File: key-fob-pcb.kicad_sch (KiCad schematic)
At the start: 1 part

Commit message: layout complete
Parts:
- removed BT1: 2468, 2468:BAT_2468, symbol 2468:2468
- added BT1: AAAx2, Connector_PinHeader_2.54mm:PinHeader_1x02_P2.54mm_Vertical, symbol Device:Battery
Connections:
- net ADC/VIN: now also BT1.1 (+)
- net GND: now also BT1.2 (-)
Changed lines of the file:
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@@
   (junction (at 62.23 46.99) (diameter 0) (color 0 0 0 0)
   )
-  (junction (at 62.23 64.77) (diameter 0) (color 0 0 0 0)
+  (junction (at 62.23 59.69) (diameter 0) (color 0 0 0 0)
   )
   (junction (at 80.01 46.99) (diameter 0) (color 0 0 0 0)
@@
     (stroke (width 0) (type default))
   )
-  (wire (pts (xy 59.69 64.77) (xy 62.23 64.77))
+  (wire (pts (xy 59.69 59.69) (xy 62.23 59.69))
     (stroke (width 0) (type default))
   )
@@
     (stroke (width 0) (type default))
   )
-  (wire (pts (xy 62.23 63.5) (xy 62.23 64.77))
+  (wire (pts (xy 62.23 58.42) (xy 62.23 59.69))
     (stroke (width 0) (type default))
   )
@@
     (stroke (width 0) (type default))
   )
-  (wire (pts (xy 62.23 64.77) (xy 62.23 66.04))
+  (wire (pts (xy 62.23 59.69) (xy 62.23 60.96))
     (stroke (width 0) (type default))
   )
@@
     (effects (font (size 1.27 1.27)) (justify right bottom))
   )
-  (symbol (lib_id "2468:2468") (at 62.23 55.88 270) (unit 1)
-    (in_bom yes) (on_board yes) (dnp no) (fields_autoplaced)
-    (property "Reference" "BT1" (at 66.04 53.975 90)
-      (effects (font (size 1.27 1.27)) (justify left))
-    )
-    (property "Value" "2468" (at 66.04 56.515 90)
-      (effects (font (size 1.27 1.27)) (justify left))
-    )
-    (property "Footprint" "2468:BAT_2468" (at 62.23 55.88 0)
-      (effects (font (size 1.27 1.27)) (justify bottom) hide)
-    )
-    (property "Datasheet" "" (at 62.23 55.88 0)
-      (effects (font (size 1.27 1.27)) hide)
-    )
-    (property "PARTREV" "D" (at 62.23 55.88 0)
-      (effects (font (size 1.27 1.27)) (justify bottom) hide)
-    )
-    (property "STANDARD" "Manufacturer Recommendations" (at 62.23 55.88 0)
-      (effects (font (size 1.27 1.27)) (justify bottom) hide)
-    )
-    (property "SNAPEDA_PN" "2468" (at 62.23 55.88 0)
-      (effects (font (size 1.27 1.27)) (justify bottom) hide)
-    )
-    (property "MAXIMUM_PACKAGE_HEIGHT" "13.25" (at 62.23 55.88 0)
-      (effects (font (size 1.27 1.27)) (justify bottom) hide)
-    )
-    (property "MANUFACTURER" "Keystone" (at 62.23 55.88 0)
-      (effects (font (size 1.27 1.27)) (justify bottom) hide)
-    )
-    (pin "N")
-    (pin "P")
+  (symbol (lib_id "Device:Battery") (at 62.23 53.34 0) (unit 1)
+    (in_bom yes) (on_board yes) (dnp no) (fields_autoplaced)
+    (property "Reference" "BT1" (at 66.04 51.4985 0)
+      (effects (font (size 1.27 1.27)) (justify left))
+    )
+    (property "Value" "AAAx2" (at 66.04 54.0385 0)
+      (effects (font (size 1.27 1.27)) (justify left))
+    )
+    (property "Footprint" "Connector_PinHeader_2.54mm:PinHeader_1x02_P2.54mm_Vertical" (at 62.23 51.816 90)
+      (effects (font (size 1.27 1.27)) hide)
+    )
+    (property "Datasheet" "~" (at 62.23 51.816 90)
+      (effects (font (size 1.27 1.27)) hide)
+    )
+    (pin "1")
+    (pin "2")
     (instances
       (project "key-fob-pcb"
@@
     )
   )
-  (symbol (lib_id "power:PWR_FLAG") (at 59.69 64.77 90) (unit 1)
-    (in_bom yes) (on_board yes) (dnp no) (fields_autoplaced)
-    (property "Reference" "#FLG02" (at 57.785 64.77 0)
-      (effects (font (size 1.27 1.27)) hide)
-    )
-    (property "Value" "PWR_FLAG" (at 55.88 64.77 90)
-      (effects (font (size 1.27 1.27)) (justify left))
-    )
-    (property "Footprint" "" (at 59.69 64.77 0)
-      (effects (font (size 1.27 1.27)) hide)
-    )
-    (property "Datasheet" "~" (at 59.69 64.77 0)
+  (symbol (lib_id "power:PWR_FLAG") (at 59.69 59.69 90) (unit 1)
+    (in_bom yes) (on_board yes) (dnp no) (fields_autoplaced)
+    (property "Reference" "#FLG02" (at 57.785 59.69 0)
+      (effects (font (size 1.27 1.27)) hide)
+    )
+    (property "Value" "PWR_FLAG" (at 55.88 59.69 90)
+      (effects (font (size 1.27 1.27)) (justify left))
+    )
+    (property "Footprint" "" (at 59.69 59.69 0)
+      (effects (font (size 1.27 1.27)) hide)
+    )
+    (property "Datasheet" "~" (at 59.69 59.69 0)
       (effects (font (size 1.27 1.27)) hide)
     )
@@
     )
   )
-  (symbol (lib_id "power:GND") (at 62.23 66.04 0) (unit 1)
-    (in_bom yes) (on_board yes) (dnp no) (fields_autoplaced)
-    (property "Reference" "#PWR01" (at 62.23 72.39 0)
-      (effects (font (size 1.27 1.27)) hide)
-    )
-    (property "Value" "GND" (at 62.23 71.12 0)
+  (symbol (lib_id "power:GND") (at 62.23 60.96 0) (unit 1)
+    (in_bom yes) (on_board yes) (dnp no) (fields_autoplaced)
+    (property "Reference" "#PWR01" (at 62.23 67.31 0)
+      (effects (font (size 1.27 1.27)) hide)
+    )
+    (property "Value" "GND" (at 62.23 66.04 0)
       (effects (font (size 1.27 1.27)))
     )
-    (property "Footprint" "" (at 62.23 66.04 0)
-      (effects (font (size 1.27 1.27)) hide)
-    )
-    (property "Datasheet" "" (at 62.23 66.04 0)
-      (effects (font (size 1.27 1.27)) hide)
-    )
+    (property "Footprint" "" (at 62.23 60.96 0)
+      (effects (font (size 1.27 1.27)) hide)
+    )
+    (property "Datasheet" "" (at 62.23 60.96 0)
+      (effects (font (size 1.27 1.27)) hide)
+    )

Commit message: generate fab files
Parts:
- BT1: now left out of the parts list
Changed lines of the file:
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@@
   )
   (symbol (lib_id "Device:Battery") (at 62.23 53.34 0) (unit 1)
-    (in_bom yes) (on_board yes) (dnp no) (fields_autoplaced)
+    (in_bom no) (on_board yes) (dnp no) (fields_autoplaced)
     (property "Reference" "BT1" (at 66.04 51.4985 0)
       (effects (font (size 1.27 1.27)) (justify left))

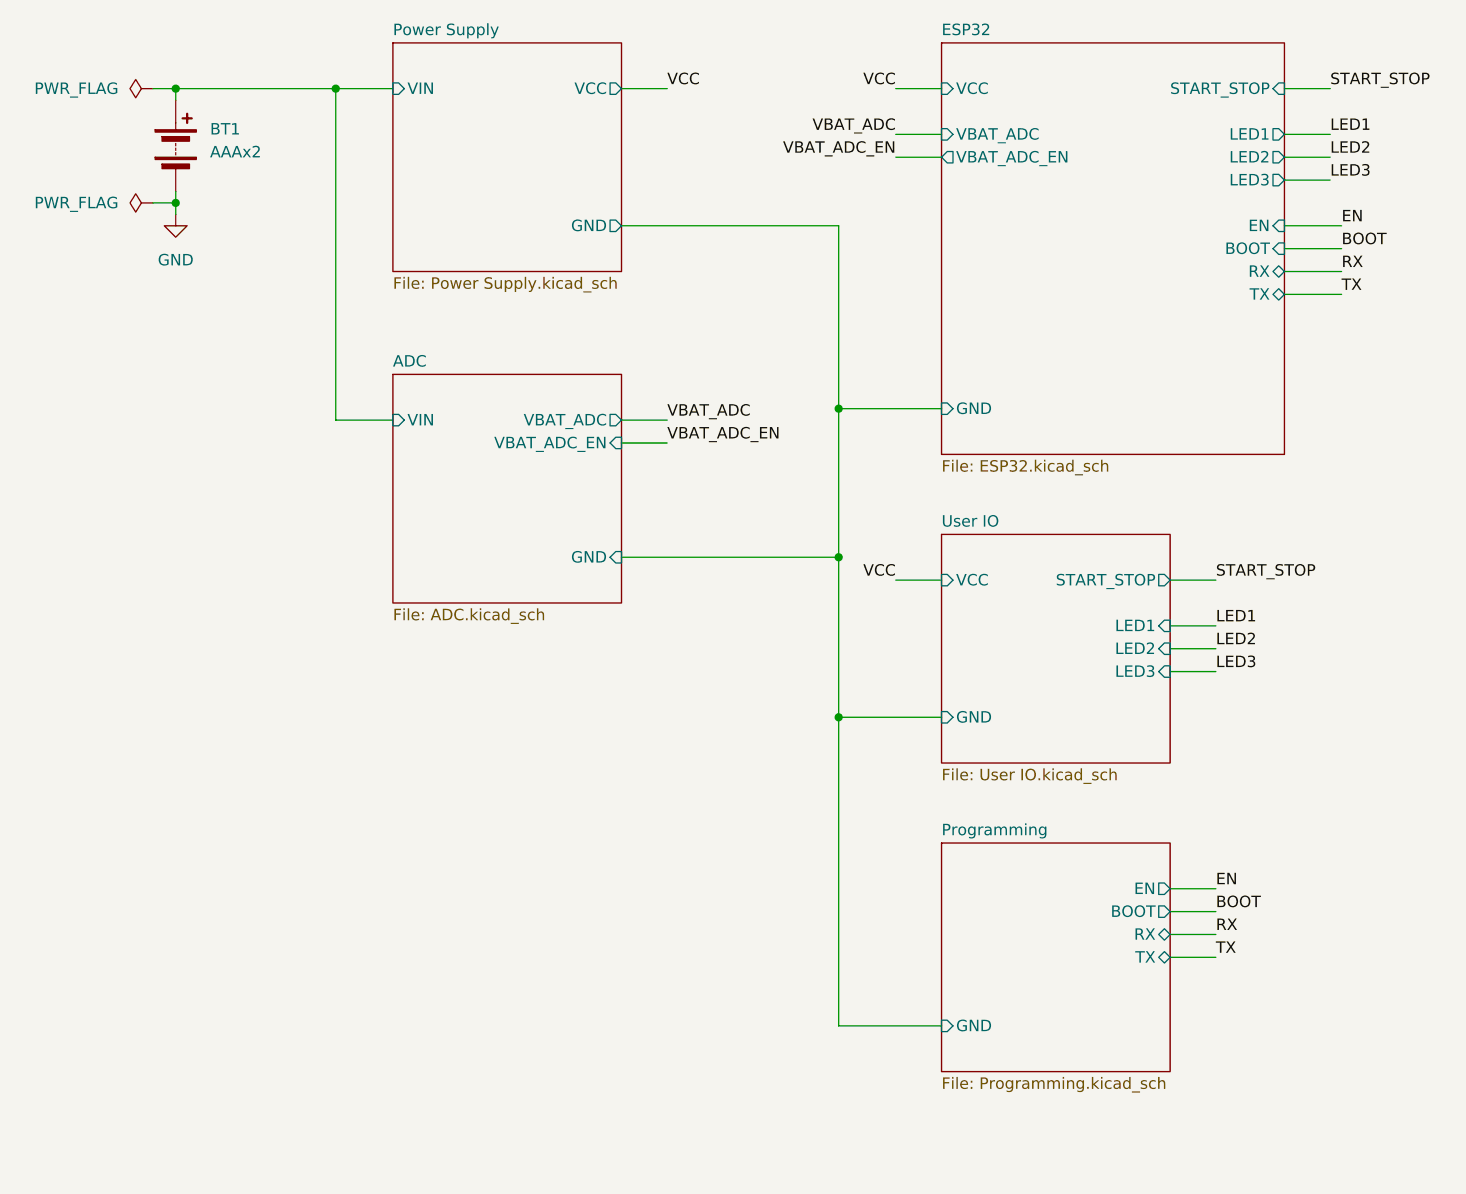
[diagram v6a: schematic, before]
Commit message: replace GND heriarchical labels with GND symbols
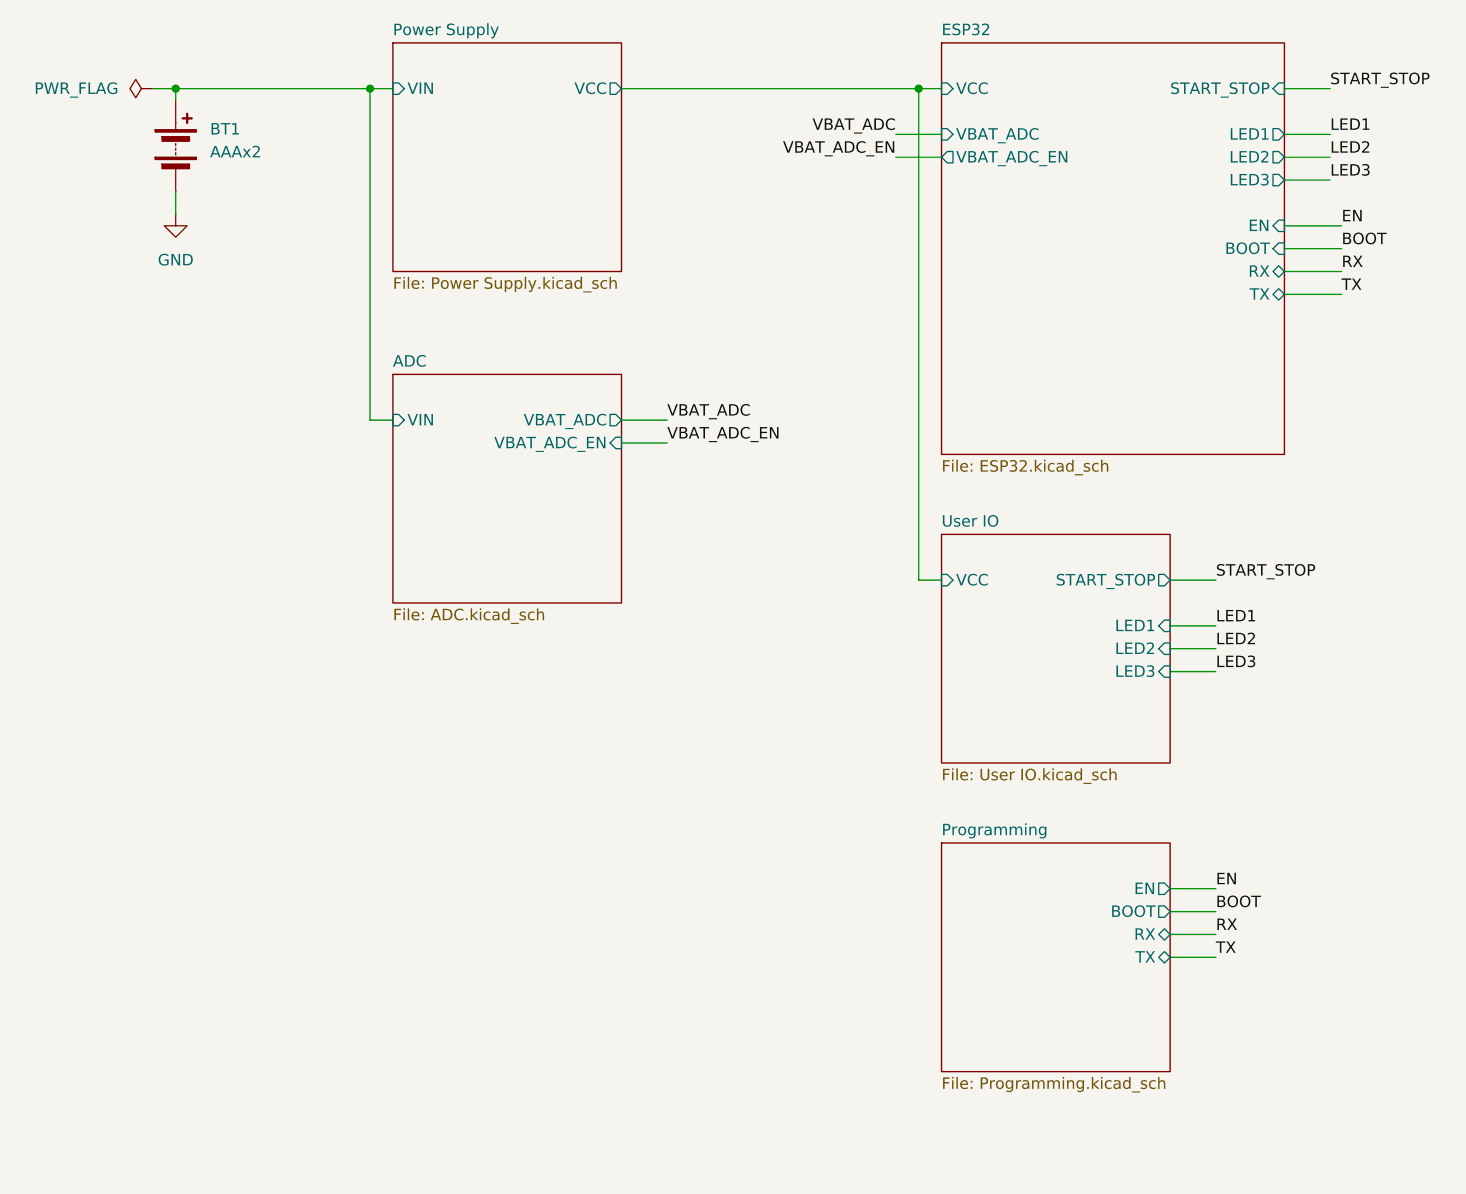
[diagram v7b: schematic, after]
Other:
- sheet ADC ports: added none; removed GND
- sheet ESP32 ports: added none; removed GND
- sheet Power Supply ports: added none; removed GND
- sheet Programming ports: added none; removed GND
- sheet User IO ports: added none; removed GND
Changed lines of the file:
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@@
     (company "J2B")
   )
-  (junction (at 135.89 82.55) (diameter 0) (color 0 0 0 0)
-  )
-  (junction (at 135.89 116.84) (diameter 0) (color 0 0 0 0)
-  )
-  (junction (at 135.89 99.06) (diameter 0) (color 0 0 0 0)
-  )
   (junction (at 62.23 46.99) (diameter 0) (color 0 0 0 0)
   )
-  (junction (at 62.23 59.69) (diameter 0) (color 0 0 0 0)
-  )
-  (junction (at 80.01 46.99) (diameter 0) (color 0 0 0 0)
-  )
-  (wire (pts (xy 80.01 83.82) (xy 80.01 46.99))
+  (junction (at 144.78 46.99) (diameter 0) (color 0 0 0 0)
+  )
+  (junction (at 83.82 46.99) (diameter 0) (color 0 0 0 0)
+  )
+  (wire (pts (xy 83.82 83.82) (xy 83.82 46.99))
     (stroke (width 0) (type default))
   )
@@
     (stroke (width 0) (type default))
   )
-  (wire (pts (xy 111.76 46.99) (xy 116.84 46.99))
-    (stroke (width 0) (type default))
-  )
-  (wire (pts (xy 59.69 59.69) (xy 62.23 59.69))
+  (wire (pts (xy 111.76 46.99) (xy 144.78 46.99))
     (stroke (width 0) (type default))
   )
@@
     (stroke (width 0) (type default))
   )
-  (wire (pts (xy 111.76 62.23) (xy 135.89 62.23))
-    (stroke (width 0) (type default))
-  )
-  (wire (pts (xy 135.89 62.23) (xy 135.89 82.55))
-    (stroke (width 0) (type default))
-  )
-  (wire (pts (xy 135.89 151.13) (xy 135.89 116.84))
-    (stroke (width 0) (type default))
-  )
-  (wire (pts (xy 111.76 99.06) (xy 135.89 99.06))
-    (stroke (width 0) (type default))
-  )
-  (wire (pts (xy 86.36 46.99) (xy 80.01 46.99))
+  (wire (pts (xy 86.36 46.99) (xy 83.82 46.99))
     (stroke (width 0) (type default))
   )
@@
     (stroke (width 0) (type default))
   )
-  (wire (pts (xy 142.24 101.6) (xy 147.32 101.6))
-    (stroke (width 0) (type default))
-  )
   (wire (pts (xy 172.72 138.43) (xy 177.8 138.43))
     (stroke (width 0) (type default))
@@
     (stroke (width 0) (type default))
   )
+  (wire (pts (xy 144.78 101.6) (xy 147.32 101.6))
+    (stroke (width 0) (type default))
+  )
   (wire (pts (xy 172.72 111.76) (xy 177.8 111.76))
     (stroke (width 0) (type default))
   )
-  (wire (pts (xy 135.89 82.55) (xy 135.89 99.06))
-    (stroke (width 0) (type default))
-  )
-  (wire (pts (xy 142.24 46.99) (xy 147.32 46.99))
-    (stroke (width 0) (type default))
-  )
   (wire (pts (xy 185.42 62.23) (xy 191.77 62.23))
     (stroke (width 0) (type default))
@@
     (stroke (width 0) (type default))
   )
-  (wire (pts (xy 80.01 46.99) (xy 62.23 46.99))
-    (stroke (width 0) (type default))
-  )
   (wire (pts (xy 185.42 54.61) (xy 190.5 54.61))
     (stroke (width 0) (type default))
   )
-  (wire (pts (xy 62.23 58.42) (xy 62.23 59.69))
-    (stroke (width 0) (type default))
-  )
-  (wire (pts (xy 86.36 83.82) (xy 80.01 83.82))
+  (wire (pts (xy 62.23 58.42) (xy 62.23 60.96))
+    (stroke (width 0) (type default))
+  )
+  (wire (pts (xy 86.36 83.82) (xy 83.82 83.82))
     (stroke (width 0) (type default))
   )
@@
     (stroke (width 0) (type default))
   )
+  (wire (pts (xy 144.78 46.99) (xy 144.78 101.6))
+    (stroke (width 0) (type default))
+  )
+  (wire (pts (xy 62.23 46.99) (xy 83.82 46.99))
+    (stroke (width 0) (type default))
+  )
   (wire (pts (xy 62.23 46.99) (xy 62.23 48.26))
     (stroke (width 0) (type default))
   )
-  (wire (pts (xy 147.32 151.13) (xy 135.89 151.13))
-    (stroke (width 0) (type default))
-  )
   (wire (pts (xy 172.72 135.89) (xy 177.8 135.89))
     (stroke (width 0) (type default))
   )
-  (wire (pts (xy 135.89 116.84) (xy 147.32 116.84))
-    (stroke (width 0) (type default))
-  )
   (wire (pts (xy 185.42 57.15) (xy 190.5 57.15))
     (stroke (width 0) (type default))
@@
     (stroke (width 0) (type default))
   )
-  (wire (pts (xy 62.23 59.69) (xy 62.23 60.96))
-    (stroke (width 0) (type default))
-  )
-  (wire (pts (xy 135.89 99.06) (xy 135.89 116.84))
-    (stroke (width 0) (type default))
-  )
-  (wire (pts (xy 135.89 82.55) (xy 147.32 82.55))
+  (wire (pts (xy 144.78 46.99) (xy 147.32 46.99))
     (stroke (width 0) (type default))
   )
@@
     (effects (font (size 1.27 1.27)) (justify left bottom))
   )
-  (label "VCC" (at 142.24 46.99 180) (fields_autoplaced)
-    (effects (font (size 1.27 1.27)) (justify right bottom))
-  )
   (label "LED3" (at 177.8 111.76 0) (fields_autoplaced)
     (effects (font (size 1.27 1.27)) (justify left bottom))
   )
-  (label "VCC" (at 116.84 46.99 0) (fields_autoplaced)
-    (effects (font (size 1.27 1.27)) (justify left bottom))
-  )
   (label "LED2" (at 190.5 54.61 0) (fields_autoplaced)
     (effects (font (size 1.27 1.27)) (justify left bottom))
@@
   (label "START_STOP" (at 190.5 46.99 0) (fields_autoplaced)
     (effects (font (size 1.27 1.27)) (justify left bottom))
-  )
-  (label "VCC" (at 142.24 101.6 180) (fields_autoplaced)
-    (effects (font (size 1.27 1.27)) (justify right bottom))
   )
   (label "EN" (at 191.77 62.23 0) (fields_autoplaced)
@@
     )
   )
-  (symbol (lib_id "power:PWR_FLAG") (at 59.69 59.69 90) (unit 1)
-    (in_bom yes) (on_board yes) (dnp no) (fields_autoplaced)
-    (property "Reference" "#FLG02" (at 57.785 59.69 0)
-      (effects (font (size 1.27 1.27)) hide)
-    )
-    (property "Value" "PWR_FLAG" (at 55.88 59.69 90)
-      (effects (font (size 1.27 1.27)) (justify left))
-    )
-    (property "Footprint" "" (at 59.69 59.69 0)
-      (effects (font (size 1.27 1.27)) hide)
-    )
-    (property "Datasheet" "~" (at 59.69 59.69 0)
-      (effects (font (size 1.27 1.27)) hide)
-    )
-    (pin "1")
-    (instances
-      (project "key-fob-pcb"
-        (path "/b002c3bf-fc58-4993-80f7-7914d3aa1ac9"
-          (reference "#FLG02") (unit 1)
-        )
-      )
-    )
-  )
   (symbol (lib_id "power:GND") (at 62.23 60.96 0) (unit 1)
     (in_bom yes) (on_board yes) (dnp no) (fields_autoplaced)
@@
       (effects (font (size 1.27 1.27)) (justify left top))
     )
-    (pin "GND" input (at 147.32 116.84 180)
-      (effects (font (size 1.27 1.27)) (justify left))
-    )
     (pin "START_STOP" output (at 172.72 101.6 0)
       (effects (font (size 1.27 1.27)) (justify right))
@@
       (effects (font (size 1.27 1.27)) (justify left))
     )
-    (pin "GND" input (at 147.32 82.55 180)
-      (effects (font (size 1.27 1.27)) (justify left))
-    )
     (pin "TX" bidirectional (at 185.42 69.85 0)
       (effects (font (size 1.27 1.27)) (justify right))
@@
       (effects (font (size 1.27 1.27)) (justify left top))
     )
-    (pin "GND" input (at 111.76 99.06 0)
-      (effects (font (size 1.27 1.27)) (justify right))
-    )
     (pin "VBAT_ADC" output (at 111.76 83.82 0)
       (effects (font (size 1.27 1.27)) (justify right))
@@
       (effects (font (size 1.27 1.27)) (justify right))
     )
-    (pin "GND" output (at 111.76 62.23 0)
-      (effects (font (size 1.27 1.27)) (justify right))
-    )
     (pin "VIN" input (at 86.36 46.99 180)
       (effects (font (size 1.27 1.27)) (justify left))
@@
       (effects (font (size 1.27 1.27)) (justify left top))
     )
-    (pin "GND" input (at 147.32 151.13 180)
-      (effects (font (size 1.27 1.27)) (justify left))
-    )
     (pin "RX" bidirectional (at 172.72 140.97 0)
